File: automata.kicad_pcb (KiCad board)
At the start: 2 copper layers, 246.4 x 127 mm, 124 parts, among them J1 Barrel_Jack, J2 LCD, J3 ICSP, J4 SERIAL, Q1 2N2907, Q2 IRF5305PBF, SW1 INPUT_SEL, SW2 SW_DIP_x08, SW3 Reset, U1 4006, U10 TLC555, U11 4040, U12 74HC11, U13 4024, U14 74HC139, U15 74HC04, U16 4053, U17 74HC164, U18 74HC164, U19 74HC164, U2 74HC04, U20 74HC164, U21 74HC164, U22 74HC164, U23 74HC164, U24 74HC164, U25 4013, U26 ATmega328-PU, U27 MCP1700-3302E_TO92, U3 4030, U4 74HC164, U5 TC40H373, U6 TC40H373, U7 74HC165, U8 4512, U9 TLC555, X1 16MHz

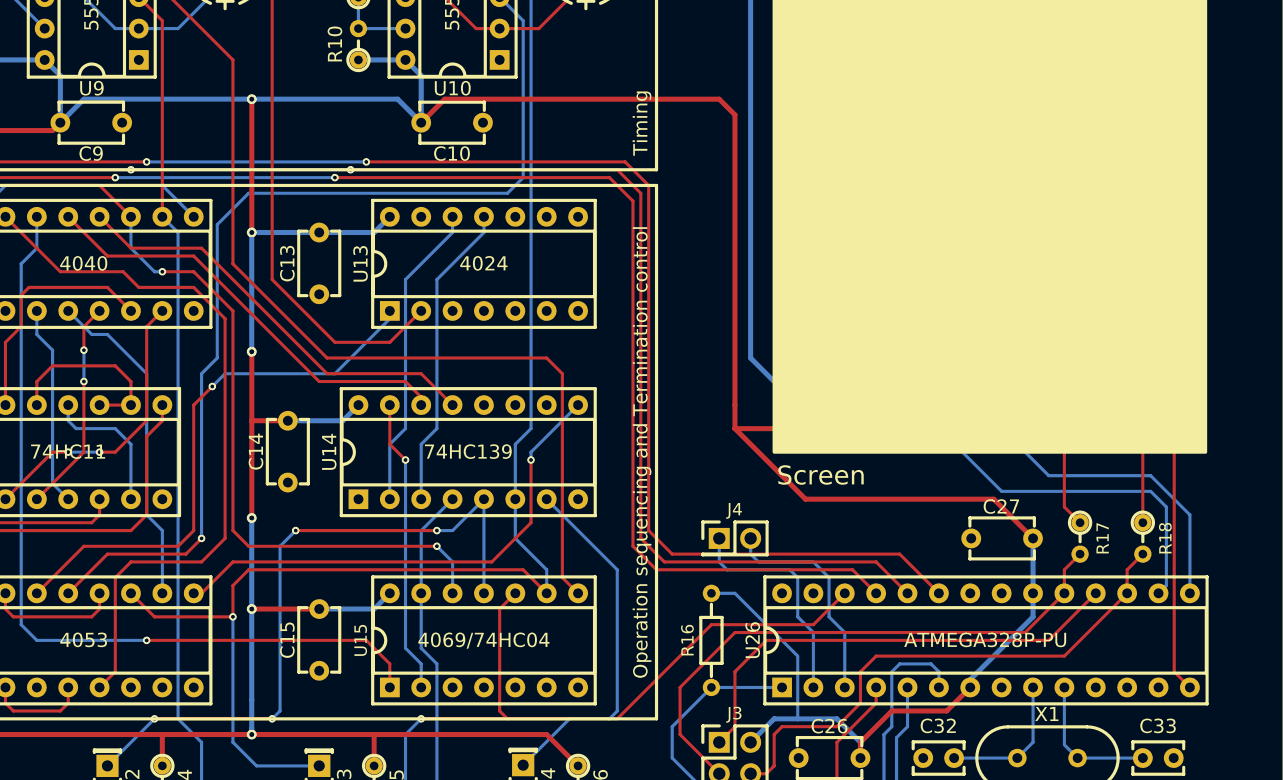
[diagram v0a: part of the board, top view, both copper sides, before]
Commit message: Remove rescue libs and fixed MC14557 symbol error
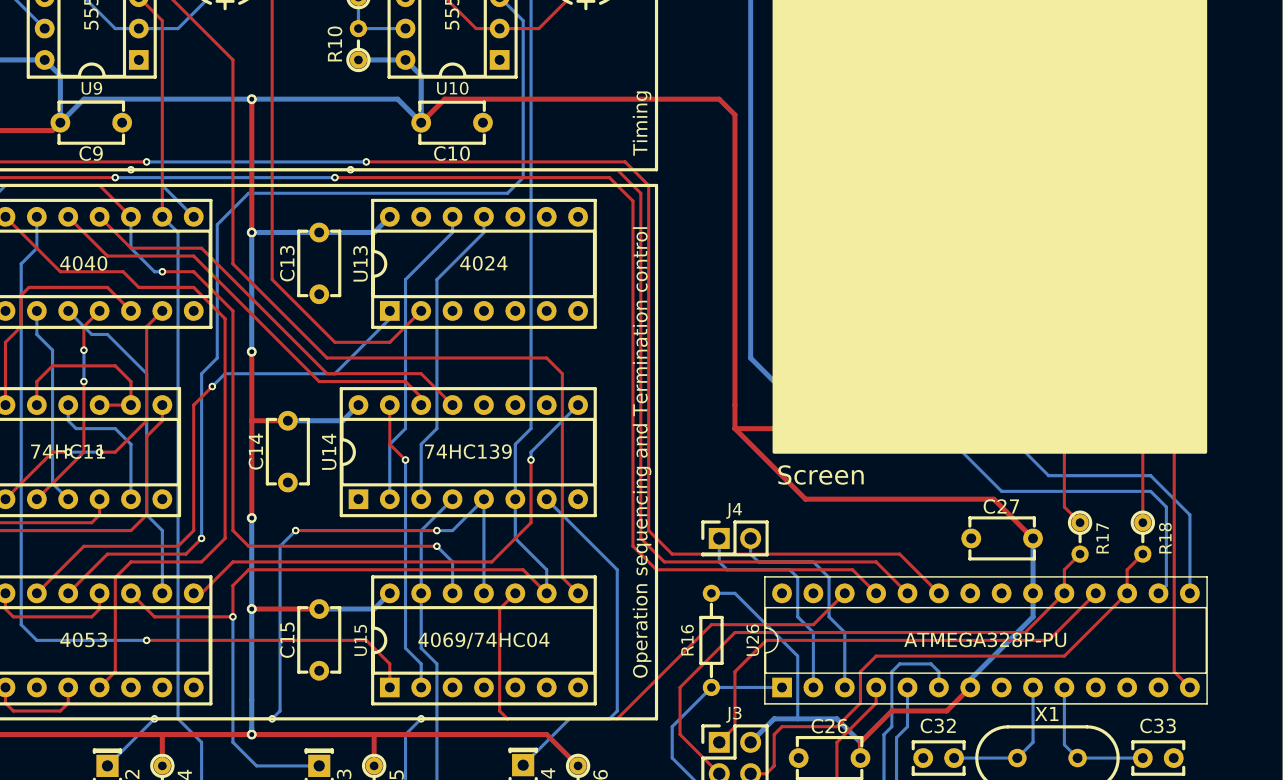
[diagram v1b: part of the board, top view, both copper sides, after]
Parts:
- U10, U9: value TLC555 -> TLC555-Timer; footprint Housings_DIP:DIP-8_W7.62mm_Socket -> Package_DIP:DIP-8_W7.62mm_Socket
- U26: footprint Housings_DIP:DIP-28_W7.62mm_Socket -> Package_DIP:DIP-28_W7.62mm_Socket

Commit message: Rev 3 design update for standard version
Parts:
- removed VR1: 3362P-1-102TLF, SamacSys_Parts:3362P_1
- added RV1: 1k, SamacSys_Parts:3362P_1, F.Cu at (162.6, 46.4)
- C1, C10, C11, C12, C13, C14, C15, C16, C17, C18, C19, C2, C20, C21, C22, C23, C24, C25, C26, C27, C3, C4, C5, C6, C7, C8, C9: footprint Capacitors_THT:C_Disc_D5.1mm_W3.2mm_P5.00mm -> Capacitor_THT:C_Disc_D5.1mm_W3.2mm_P5.00mm
- C28: value 1000uF -> 100uF; footprint Capacitors_THT:CP_Radial_D10.0mm_P5.00mm -> Capacitor_THT:CP_Radial_D8.0mm_P2.50mm
- C29, C30, C32, C33, C35, C37: footprint Capacitors_THT:C_Rect_L4.0mm_W2.5mm_P2.50mm -> Capacitor_THT:C_Disc_D5.1mm_W3.2mm_P5.00mm
- C31: footprint Capacitors_THT:CP_Radial_D5.0mm_P2.00mm -> Capacitor_THT:CP_Radial_D5.0mm_P2.00mm
- C34, C36: footprint Capacitors_THT:CP_Radial_D6.3mm_P2.50mm -> Capacitor_THT:CP_Radial_D8.0mm_P2.50mm
- D1, D2, D3, D4, D5, D6, D7: footprint LEDs:LED_Rectangular_W5.0mm_H2.0mm -> LED_THT:LED_Rectangular_W5.0mm_H2.0mm
- D8: footprint Diodes_THT:D_DO-35_SOD27_P7.62mm_Horizontal -> Diode_THT:D_DO-35_SOD27_P7.62mm_Horizontal
- H1, H2, H3, H4: footprint Mounting_Holes:MountingHole_2.2mm_M2_Pad -> MountingHole:MountingHole_2.2mm_M2_Pad
- J1: footprint Connectors:BARREL_JACK -> Connector_BarrelJack:BarrelJack_Horizontal
- J2: footprint Pin_Headers:Pin_Header_Straight_1x08_Pitch2.54mm -> Connector_PinHeader_2.54mm:PinHeader_1x08_P2.54mm_Vertical
- J3: footprint Pin_Headers:Pin_Header_Straight_2x03_Pitch2.54mm -> Connector_PinHeader_2.54mm:PinHeader_2x03_P2.54mm_Vertical
- J4: footprint Pin_Headers:Pin_Header_Straight_2x01_Pitch2.54mm -> Connector_PinHeader_2.54mm:PinHeader_2x01_P2.54mm_Vertical
- Q1, U27: footprint TO_SOT_Packages_THT:TO-92_Inline_Narrow_Oval -> Package_TO_SOT_THT:TO-92_Inline
- Q2: footprint TO_SOT_Packages_THT:TO-220-3_Horizontal -> Package_TO_SOT_THT:TO-220-3_Horizontal_TabDown
- R1, R12, R13, R14, R16, R2: footprint Resistors_THT:R_Axial_DIN0204_L3.6mm_D1.6mm_P7.62mm_Horizontal -> Resistor_THT:R_Axial_DIN0204_L3.6mm_D1.6mm_P7.62mm_Horizontal
- R10, R11, R9: footprint Resistors_THT:R_Axial_DIN0204_L3.6mm_D1.6mm_P2.54mm_Vertical -> Resistor_THT:R_Axial_DIN0204_L3.6mm_D1.6mm_P2.54mm_Vertical
- R15, R8: value 330 -> 470; footprint Resistors_THT:R_Axial_DIN0204_L3.6mm_D1.6mm_P7.62mm_Horizontal -> Resistor_THT:R_Axial_DIN0204_L3.6mm_D1.6mm_P7.62mm_Horizontal
- R17, R18, R3, R4, R5, R6, R7: value 330 -> 470; footprint Resistors_THT:R_Axial_DIN0204_L3.6mm_D1.6mm_P2.54mm_Vertical -> Resistor_THT:R_Axial_DIN0204_L3.6mm_D1.6mm_P2.54mm_Vertical
- RN1, RN2, RN3, RN4, RN5, RN6, RN7, RN8, RN9: footprint Resistors_THT:R_Array_SIP9 -> Resistor_THT:R_Array_SIP9
- SW2: footprint Housings_DIP:DIP-16_W7.62mm_Socket -> Button_Switch_THT:SW_DIP_SPSTx08_Slide_9.78x22.5mm_W7.62mm_P2.54mm
- SW3: footprint Buttons_Switches_THT:SW_PUSH_6mm -> Button_Switch_THT:SW_PUSH_6mm
- U1: value 4006 -> 74HC164; footprint Housings_DIP:DIP-14_W7.62mm_Socket -> Package_DIP:DIP-14_W7.62mm_Socket
- U11, U14, U16, U7, U8: footprint Housings_DIP:DIP-16_W7.62mm_Socket -> Package_DIP:DIP-16_W7.62mm_Socket
- U12, U13, U15, U17, U18, U19, U20, U21, U22, U23, U24, U25, U4: footprint Housings_DIP:DIP-14_W7.62mm_Socket -> Package_DIP:DIP-14_W7.62mm_Socket
- U2: value 74HC04 -> 4077; footprint Housings_DIP:DIP-14_W7.62mm_Socket -> Package_DIP:DIP-14_W7.62mm_Socket
- U3: value 4030 -> 74HC164; footprint Housings_DIP:DIP-14_W7.62mm_Socket -> Package_DIP:DIP-14_W7.62mm_Socket
- U5, U6: value TC40H373 -> 74HC373; footprint Housings_DIP:DIP-20_W7.62mm_Socket -> Package_DIP:DIP-20_W7.62mm_Socket
- X1: footprint Crystals:Crystal_HC49-4H_Vertical -> Crystal:Crystal_HC49-4H_Vertical
- moved C36 3.91 mm to (215.5, 48.3)
- moved C34 3.89 mm to (186.2, 48.3)
- moved C32 2.54 mm to (239.4, 107.3)
- moved C37 1.40 mm to (201.3, 39.0)
- moved C35 1.40 mm to (172.1, 39.0)
- moved C30 1.37 mm to (92.8, 43.2)
- moved C29 1.33 mm to (80.4, 43.2)
- moved C28 1.31 mm to (68.6, 44.3)
- moved C22 0.64 mm to (189.9, 123.8)
- moved C24 0.64 mm to (243.2, 123.8)
- moved U22 0.64 mm to (195.6, 130.2)
- moved C21 0.63 mm to (163.2, 123.8)
- moved C23 0.63 mm to (216.5, 123.8)
- moved U21 0.63 mm to (168.9, 130.2)
- moved U23 0.63 mm to (222.2, 130.2)
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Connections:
- U1 pad 12: Net-(U1-Pad1) -> Net-(U1-Pad12)
- U1 pad 2: Net-(U1-Pad2) -> Net-(U1-Pad1)
- U1 pad 3: MCLK -> Net-(U1-Pad3)
- U1 pad 4: Net-(U1-Pad10) -> Net-(U1-Pad4)
- U1 pad 8: Net-(U1-Pad8) -> MCLK
- U1 pad 9: Net-(U1-Pad5) -> +5V
- U2 pad 11: GNDREF -> Net-(U2-Pad11)
- U2 pad 12: Net-(U2-Pad12) -> GNDREF
- U2 pad 3: GNDREF -> Net-(U1-Pad1)
- U2 pad 6: Net-(U2-Pad6) -> GNDREF
- U2 pad 8: Net-(U2-Pad8) -> GNDREF
- U3 pad 12: GNDREF -> Net-(U3-Pad12)
- U3 pad 13: GNDREF -> Net-(U3-Pad13)
- U3 pad 2: Net-(U1-Pad5) -> Net-(U1-Pad13)
- U3 pad 3: Net-(U2-Pad1) -> Net-(U3-Pad3)
- U3 pad 4: Net-(U1-Pad6) -> Net-(U3-Pad4)
- U3 pad 5: Net-(U1-Pad10) -> Net-(U3-Pad5)
- U3 pad 6: Net-(U2-Pad2) -> Net-(U3-Pad6)
- U3 pad 8: GNDREF -> MCLK
- U3 pad 9: GNDREF -> +5V
- U4 pad 1: Net-(U1-Pad6) -> Net-(U3-Pad13)
- U4 pad 12: Net-(U4-Pad12) -> Net-(U2-Pad2)
- U4 pad 2: Net-(U1-Pad6) -> Net-(U3-Pad13)
- U4 pad 4: Net-(U4-Pad4) -> Net-(U2-Pad1)
- U5 pad 17: Net-(U4-Pad12) -> Net-(U2-Pad2)
- U5 pad 4: Net-(U4-Pad4) -> Net-(U2-Pad1)
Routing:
- net +5V: track 1237.7 -> 1288.4 mm, vias 13 -> 14
- net Net-(U1-Pad6): track 44.5 -> 0.00 mm, vias 1 -> 0
- net Net-(U4-Pad12): track 42.0 -> 0.00 mm
- net Net-(U4-Pad4): track 39.5 -> 0.00 mm
- net Net-(U3-Pad13): track 0.00 -> 30.7 mm
- net Net-(U2-Pad1): track 29.0 -> 57.9 mm
- net Net-(U2-Pad2): track 23.6 -> 50.7 mm
- net Net-(U1-Pad5): track 27.1 -> 0.00 mm
- net Net-(U1-Pad1): track 9.72 -> 35.7 mm
- net Net-(U1-Pad10): track 25.0 -> 0.00 mm
- net MCLK: track 437.1 -> 443.4 mm, vias 6 -> 4
- net ~RST: track 308.2 -> 312.7 mm
- net Net-(U1-Pad13): track 23.9 -> 26.5 mm
- net Net-(BAR7-Pad1): track 77.5 -> 79.8 mm
- net Net-(BAR7-Pad2): track 41.7 -> 42.7 mm
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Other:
- board text added: "4077"
- board text added: "CMOS Elementary Automata Visualization Board Rev. 3"
- board text added: "ICSP"
- board text added: "Serial"
- board text removed: "4006"
- board text removed: "4030/4070"
- board text removed: "CMOS Elementary Automata Visualization Board Rev. 2"

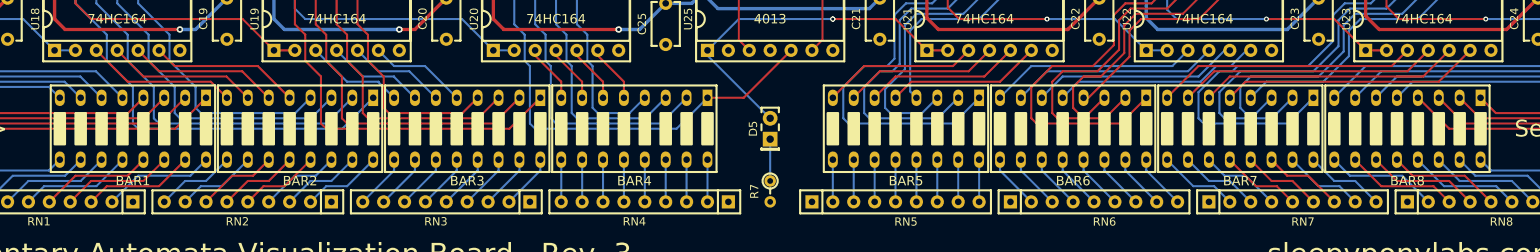
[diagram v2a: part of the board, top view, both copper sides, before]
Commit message: Changed LED bargraphs to 10-bar variant
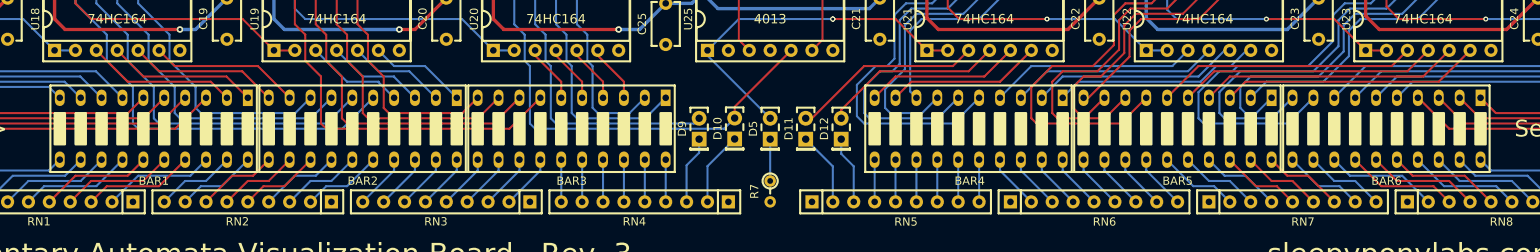
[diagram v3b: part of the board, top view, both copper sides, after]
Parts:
- removed BAR7, BAR8: BARGRAPH8, automata:BARGRAPH_DIP_8
- added D10: B31, LED_THT:LED_Rectangular_W5.0mm_H2.0mm, F.Cu at (145.5, 140.9)
- added D11: B33, LED_THT:LED_Rectangular_W5.0mm_H2.0mm, F.Cu at (154.2, 141.0)
- added D12: B34, LED_THT:LED_Rectangular_W5.0mm_H2.0mm, F.Cu at (158.5, 141.0)
- added D9: B30, LED_THT:LED_Rectangular_W5.0mm_H2.0mm, F.Cu at (141.2, 141.0)
- BAR1, BAR2, BAR3, BAR4, BAR5, BAR6: value BARGRAPH8 -> BARGRAPH10; footprint automata:BARGRAPH_DIP_8 -> automata:BARGRAPH_DIP_10
- D5: value CENTER -> B32
- moved BAR4 40.6 mm to (174.0, 139.7)
- moved BAR6 38.1 mm to (224.8, 139.7)
- moved BAR5 33.0 mm to (199.4, 139.7)
- moved BAR3 12.7 mm to (125.7, 139.7)
- moved BAR2 7.62 mm to (100.3, 139.7)
- moved BAR1 2.54 mm to (74.9, 139.7)
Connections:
- BAR6 pad 1: Net-(BAR6-Pad1) -> SENSE_A
- BAR6 pad 2: Net-(BAR6-Pad2) -> SENSE_B
- BAR6 pad 3: Net-(BAR6-Pad3) -> SENSE_C
- RN1 pad 2: Net-(BAR1-Pad16) -> Net-(BAR1-Pad18)
- RN1 pad 3: Net-(BAR1-Pad15) -> Net-(BAR1-Pad17)
- RN1 pad 4: Net-(BAR1-Pad14) -> Net-(BAR1-Pad16)
- RN1 pad 5: Net-(BAR1-Pad13) -> Net-(BAR1-Pad15)
- RN1 pad 6: Net-(BAR1-Pad12) -> Net-(BAR1-Pad14)
- RN1 pad 7: Net-(BAR1-Pad11) -> Net-(BAR1-Pad13)
- RN1 pad 8: Net-(BAR1-Pad10) -> Net-(BAR1-Pad12)
- RN1 pad 9: Net-(BAR1-Pad9) -> Net-(BAR1-Pad11)
- RN2 pad 8: Net-(BAR2-Pad10) -> Net-(BAR1-Pad20)
- RN2 pad 9: Net-(BAR2-Pad9) -> Net-(BAR1-Pad19)
- RN3 pad 2: Net-(BAR3-Pad16) -> Net-(BAR3-Pad14)
- RN3 pad 3: Net-(BAR3-Pad15) -> Net-(BAR3-Pad13)
- RN3 pad 4: Net-(BAR3-Pad14) -> Net-(BAR3-Pad12)
- RN3 pad 5: Net-(BAR3-Pad13) -> Net-(BAR3-Pad11)
- RN3 pad 6: Net-(BAR3-Pad12) -> Net-(BAR2-Pad20)
- RN3 pad 7: Net-(BAR3-Pad11) -> Net-(BAR2-Pad19)
- RN3 pad 8: Net-(BAR3-Pad10) -> Net-(BAR2-Pad18)
- RN3 pad 9: Net-(BAR3-Pad9) -> Net-(BAR2-Pad17)
- RN4 pad 2: Net-(BAR4-Pad16) -> Net-(D10-Pad1)
- RN4 pad 3: Net-(BAR4-Pad15) -> Net-(D9-Pad1)
- RN4 pad 4: Net-(BAR4-Pad14) -> Net-(BAR3-Pad20)
- RN4 pad 5: Net-(BAR4-Pad13) -> Net-(BAR3-Pad19)
- RN4 pad 6: Net-(BAR4-Pad12) -> Net-(BAR3-Pad18)
- RN4 pad 7: Net-(BAR4-Pad11) -> Net-(BAR3-Pad17)
- RN4 pad 8: Net-(BAR4-Pad10) -> Net-(BAR3-Pad16)
- RN4 pad 9: Net-(BAR4-Pad9) -> Net-(BAR3-Pad15)
- RN5 pad 2: Net-(BAR5-Pad9) -> Net-(D11-Pad1)
- RN5 pad 3: Net-(BAR5-Pad10) -> Net-(D12-Pad1)
- RN5 pad 4: Net-(BAR5-Pad11) -> Net-(BAR4-Pad11)
- RN5 pad 5: Net-(BAR5-Pad12) -> Net-(BAR4-Pad12)
- RN5 pad 6: Net-(BAR5-Pad13) -> Net-(BAR4-Pad13)
- RN5 pad 7: Net-(BAR5-Pad14) -> Net-(BAR4-Pad14)
- RN5 pad 8: Net-(BAR5-Pad15) -> Net-(BAR4-Pad15)
- RN5 pad 9: Net-(BAR5-Pad16) -> Net-(BAR4-Pad16)
- RN6 pad 2: Net-(BAR6-Pad9) -> Net-(BAR4-Pad17)
- RN6 pad 3: Net-(BAR6-Pad10) -> Net-(BAR4-Pad18)
- RN6 pad 4: Net-(BAR6-Pad11) -> Net-(BAR4-Pad19)
- RN6 pad 5: Net-(BAR6-Pad12) -> Net-(BAR4-Pad20)
- RN6 pad 6: Net-(BAR6-Pad13) -> Net-(BAR5-Pad11)
- RN6 pad 7: Net-(BAR6-Pad14) -> Net-(BAR5-Pad12)
- RN6 pad 8: Net-(BAR6-Pad15) -> Net-(BAR5-Pad13)
- RN6 pad 9: Net-(BAR6-Pad16) -> Net-(BAR5-Pad14)
- RN7 pad 2: Net-(BAR7-Pad9) -> Net-(BAR5-Pad15)
- RN7 pad 3: Net-(BAR7-Pad10) -> Net-(BAR5-Pad16)
- RN7 pad 4: Net-(BAR7-Pad11) -> Net-(BAR5-Pad17)
- RN7 pad 5: Net-(BAR7-Pad12) -> Net-(BAR5-Pad18)
- RN7 pad 6: Net-(BAR7-Pad13) -> Net-(BAR5-Pad19)
- RN7 pad 7: Net-(BAR7-Pad14) -> Net-(BAR5-Pad20)
- RN7 pad 8: Net-(BAR7-Pad15) -> Net-(BAR6-Pad11)
- RN7 pad 9: Net-(BAR7-Pad16) -> Net-(BAR6-Pad12)
- RN8 pad 2: Net-(BAR8-Pad9) -> Net-(BAR6-Pad13)
- RN8 pad 3: Net-(BAR8-Pad10) -> Net-(BAR6-Pad14)
- RN8 pad 4: Net-(BAR8-Pad11) -> Net-(BAR6-Pad15)
- RN8 pad 5: Net-(BAR8-Pad12) -> Net-(BAR6-Pad16)
- RN8 pad 6: Net-(BAR8-Pad13) -> Net-(BAR6-Pad17)
- RN8 pad 7: Net-(BAR8-Pad14) -> Net-(BAR6-Pad18)
- RN8 pad 8: Net-(BAR8-Pad15) -> Net-(BAR6-Pad19)
- RN8 pad 9: Net-(BAR8-Pad16) -> Net-(BAR6-Pad20)
- U17 pad 10: Net-(BAR1-Pad4) -> Net-(BAR1-Pad6)
- U17 pad 11: Net-(BAR1-Pad3) -> Net-(BAR1-Pad5)
- U17 pad 12: Net-(BAR1-Pad2) -> Net-(BAR1-Pad4)
- U17 pad 13: Net-(BAR1-Pad1) -> Net-(BAR1-Pad3)
- U17 pad 3: Net-(BAR1-Pad8) -> Net-(BAR1-Pad10)
- U17 pad 4: Net-(BAR1-Pad7) -> Net-(BAR1-Pad9)
- U17 pad 5: Net-(BAR1-Pad6) -> Net-(BAR1-Pad8)
- U17 pad 6: Net-(BAR1-Pad5) -> Net-(BAR1-Pad7)
- U18 pad 1: Net-(BAR1-Pad1) -> Net-(BAR1-Pad3)
- U18 pad 10: Net-(BAR2-Pad4) -> Net-(BAR2-Pad8)
- U18 pad 11: Net-(BAR2-Pad3) -> Net-(BAR2-Pad7)
- U18 pad 12: Net-(BAR2-Pad2) -> Net-(BAR2-Pad6)
- U18 pad 13: Net-(BAR2-Pad1) -> Net-(BAR2-Pad5)
- U18 pad 2: Net-(BAR1-Pad1) -> Net-(BAR1-Pad3)
- U18 pad 3: Net-(BAR2-Pad8) -> Net-(BAR1-Pad2)
- U18 pad 4: Net-(BAR2-Pad7) -> Net-(BAR1-Pad1)
- U18 pad 5: Net-(BAR2-Pad6) -> Net-(BAR2-Pad10)
- U18 pad 6: Net-(BAR2-Pad5) -> Net-(BAR2-Pad9)
- U19 pad 1: Net-(BAR2-Pad1) -> Net-(BAR2-Pad5)
- U19 pad 10: Net-(BAR3-Pad4) -> Net-(BAR3-Pad10)
- U19 pad 11: Net-(BAR3-Pad3) -> Net-(BAR3-Pad9)
- U19 pad 12: Net-(BAR3-Pad2) -> Net-(BAR3-Pad8)
- U19 pad 13: Net-(BAR3-Pad1) -> Net-(BAR3-Pad7)
- U19 pad 2: Net-(BAR2-Pad1) -> Net-(BAR2-Pad5)
- U19 pad 3: Net-(BAR3-Pad8) -> Net-(BAR2-Pad4)
- U19 pad 4: Net-(BAR3-Pad7) -> Net-(BAR2-Pad3)
- U19 pad 5: Net-(BAR3-Pad6) -> Net-(BAR2-Pad2)
- U19 pad 6: Net-(BAR3-Pad5) -> Net-(BAR2-Pad1)
- U20 pad 1: Net-(BAR3-Pad1) -> Net-(BAR3-Pad7)
- U20 pad 10: Net-(BAR4-Pad4) -> Net-(BAR3-Pad2)
- U20 pad 11: Net-(BAR4-Pad3) -> Net-(BAR3-Pad1)
- U20 pad 12: Net-(BAR4-Pad2) -> Net-(D9-Pad2)
- U20 pad 13: Net-(BAR4-Pad1) -> Net-(D10-Pad2)
- U20 pad 2: Net-(BAR3-Pad1) -> Net-(BAR3-Pad7)
- U20 pad 3: Net-(BAR4-Pad8) -> Net-(BAR3-Pad6)
- U20 pad 4: Net-(BAR4-Pad7) -> Net-(BAR3-Pad5)
- U20 pad 5: Net-(BAR4-Pad6) -> Net-(BAR3-Pad4)
- U20 pad 6: Net-(BAR4-Pad5) -> Net-(BAR3-Pad3)
- U21 pad 10: Net-(BAR5-Pad4) -> Net-(BAR4-Pad8)
- U21 pad 11: Net-(BAR5-Pad3) -> Net-(BAR4-Pad7)
- U21 pad 12: Net-(BAR5-Pad2) -> Net-(BAR4-Pad6)
- U21 pad 13: Net-(BAR5-Pad1) -> Net-(BAR4-Pad5)
- U21 pad 3: Net-(BAR5-Pad8) -> Net-(D11-Pad2)
- U21 pad 4: Net-(BAR5-Pad7) -> Net-(D12-Pad2)
- U21 pad 5: Net-(BAR5-Pad6) -> Net-(BAR4-Pad10)
- U21 pad 6: Net-(BAR5-Pad5) -> Net-(BAR4-Pad9)
- U22 pad 1: Net-(BAR5-Pad1) -> Net-(BAR4-Pad5)
- U22 pad 10: Net-(BAR6-Pad4) -> Net-(BAR5-Pad10)
- U22 pad 11: Net-(BAR6-Pad3) -> Net-(BAR5-Pad9)
- U22 pad 12: Net-(BAR6-Pad2) -> Net-(BAR5-Pad8)
- U22 pad 13: Net-(BAR6-Pad1) -> Net-(BAR5-Pad7)
- U22 pad 2: Net-(BAR5-Pad1) -> Net-(BAR4-Pad5)
- U22 pad 3: Net-(BAR6-Pad8) -> Net-(BAR4-Pad4)
- U22 pad 4: Net-(BAR6-Pad7) -> Net-(BAR4-Pad3)
- U22 pad 5: Net-(BAR6-Pad6) -> Net-(BAR4-Pad2)
- U22 pad 6: Net-(BAR6-Pad5) -> Net-(BAR4-Pad1)
- U23 pad 1: Net-(BAR6-Pad1) -> Net-(BAR5-Pad7)
- U23 pad 10: Net-(BAR7-Pad4) -> Net-(BAR5-Pad2)
- U23 pad 11: Net-(BAR7-Pad3) -> Net-(BAR5-Pad1)
- U23 pad 12: Net-(BAR7-Pad2) -> Net-(BAR6-Pad10)
- U23 pad 13: Net-(BAR7-Pad1) -> Net-(BAR6-Pad9)
- U23 pad 2: Net-(BAR6-Pad1) -> Net-(BAR5-Pad7)
- U23 pad 3: Net-(BAR7-Pad8) -> Net-(BAR5-Pad6)
- U23 pad 4: Net-(BAR7-Pad7) -> Net-(BAR5-Pad5)
- U23 pad 5: Net-(BAR7-Pad6) -> Net-(BAR5-Pad4)
- U23 pad 6: Net-(BAR7-Pad5) -> Net-(BAR5-Pad3)
- U24 pad 1: Net-(BAR7-Pad1) -> Net-(BAR6-Pad9)
- U24 pad 10: Net-(BAR8-Pad4) -> Net-(BAR6-Pad4)
- U24 pad 2: Net-(BAR7-Pad1) -> Net-(BAR6-Pad9)
- U24 pad 3: Net-(BAR8-Pad8) -> Net-(BAR6-Pad8)
- U24 pad 4: Net-(BAR8-Pad7) -> Net-(BAR6-Pad7)
- U24 pad 5: Net-(BAR8-Pad6) -> Net-(BAR6-Pad6)
- U24 pad 6: Net-(BAR8-Pad5) -> Net-(BAR6-Pad5)
- U25 pad 5: Net-(BAR4-Pad1) -> Net-(D10-Pad2)
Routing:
- net Net-(BAR7-Pad1): track 79.8 -> 0.00 mm, vias 1 -> 0
- net Net-(BAR6-Pad1): track 74.4 -> 0.00 mm, vias 1 -> 0
- net Net-(BAR6-Pad9): track 6.71 -> 79.8 mm, vias 0 -> 1
- net Net-(BAR1-Pad1): track 87.7 -> 18.3 mm
- net Net-(BAR2-Pad1): track 81.4 -> 11.9 mm
- net Net-(BAR3-Pad7): track 11.9 -> 77.6 mm
- net Net-(BAR4-Pad5): track 7.08 -> 70.6 mm, vias 0 -> 1
- net Net-(BAR2-Pad5): track 18.3 -> 81.4 mm
- net Net-(BAR5-Pad7): track 18.9 -> 74.4 mm, vias 0 -> 1
- net Net-(D10-Pad2): track 0.00 -> 54.1 mm
- net Net-(BAR3-Pad1): track 77.6 -> 28.8 mm
- net Net-(BAR8-Pad4): track 46.5 -> 0.00 mm
- net Net-(BAR7-Pad2): track 42.7 -> 0.00 mm
- net Net-(BAR1-Pad3): track 45.2 -> 87.7 mm
- net Net-(BAR8-Pad7): track 38.0 -> 0.00 mm
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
